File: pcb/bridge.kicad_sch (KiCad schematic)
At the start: 46 parts, among them Q4 IRFR4105, Q5 BC817, Q6 IRFR4105, Q7 BC817, Q8 IRFR4105, Q9 IRFR4105, U1 74HC04, U10 LM75B, U2 74HC04

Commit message: Export root page escription to other pages.
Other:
- company: (none) -> Model Railroader Club Brno I – KMŽ Brno I – https://kmz-brno.cz/
- title: HB22 – bridge -> HB22 – DCC booster
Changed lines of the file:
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@@
 	(paper "A4")
 	(title_block
-		(title "HB22 – bridge")
+		(title "HB22 – DCC booster")
+		(date "2025-02-20")
+		(rev "1.0")
+		(company "Model Railroader Club Brno I – KMŽ Brno I – https://kmz-brno.cz/")
+		(comment 1 "Jan Horáček")
+		(comment 2 "https://github.com/kmzbrnoI/hb22")
+		(comment 3 "https://creativecommons.org/licenses/by-sa/4.0/")
+		(comment 4 "Released under the Creative Commons Attribution-ShareAlike 4.0 License")
 	)
 	(junction

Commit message: Use normal SMD footprints, avoid handsolder.
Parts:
- C10, C11, C12, C13, C15, C8: footprint Capacitor_SMD:C_0805_2012Metric_Pad1.18x1.45mm_HandSolder -> Capacitor_SMD:C_0805_2012Metric
- R17, R18: footprint Resistor_SMD:R_2512_6332Metric_Pad1.40x3.35mm_HandSolder -> Resistor_SMD:R_2512_6332Metric
- R19, R20, R21, R22, R23, R24, R25, R26, R27, R28, R29, R31, R32, R34, R35, R36, R37, R38, R39, R40: footprint Resistor_SMD:R_0805_2012Metric_Pad1.20x1.40mm_HandSolder -> Resistor_SMD:R_0805_2012Metric
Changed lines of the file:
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@@
 			)
 		)
-		(property "Footprint" "Resistor_SMD:R_0805_2012Metric_Pad1.20x1.40mm_HandSolder"
+		(property "Footprint" "Resistor_SMD:R_0805_2012Metric"
 			(at 170.18 129.032 90)
 			(effects
@@
 			)
 		)
-		(property "Footprint" "Resistor_SMD:R_0805_2012Metric_Pad1.20x1.40mm_HandSolder"
+		(property "Footprint" "Resistor_SMD:R_0805_2012Metric"
 			(at 200.66 143.002 90)
 			(effects
@@
 			)
 		)
-		(property "Footprint" "Resistor_SMD:R_0805_2012Metric_Pad1.20x1.40mm_HandSolder"
+		(property "Footprint" "Resistor_SMD:R_0805_2012Metric"
 			(at 200.66 80.518 90)
 			(effects
@@
 			)
 		)
-		(property "Footprint" "Resistor_SMD:R_0805_2012Metric_Pad1.20x1.40mm_HandSolder"
+		(property "Footprint" "Resistor_SMD:R_0805_2012Metric"
 			(at 170.18 62.992 90)
 			(effects
@@
 			)
 		)
-		(property "Footprint" "Resistor_SMD:R_0805_2012Metric_Pad1.20x1.40mm_HandSolder"
+		(property "Footprint" "Resistor_SMD:R_0805_2012Metric"
 			(at 199.39 110.998 90)
 			(effects
@@
 			)
 		)
-		(property "Footprint" "Capacitor_SMD:C_0805_2012Metric_Pad1.18x1.45mm_HandSolder"
+		(property "Footprint" "Capacitor_SMD:C_0805_2012Metric"
 			(at 180.34 110.1852 0)
 			(effects
@@
 			)
 		)
-		(property "Footprint" "Resistor_SMD:R_0805_2012Metric_Pad1.20x1.40mm_HandSolder"
+		(property "Footprint" "Resistor_SMD:R_0805_2012Metric"
 			(at 147.32 79.248 90)
 			(effects
@@
 			)
 		)
-		(property "Footprint" "Resistor_SMD:R_0805_2012Metric_Pad1.20x1.40mm_HandSolder"
+		(property "Footprint" "Resistor_SMD:R_0805_2012Metric"
 			(at 147.32 70.612 90)
 			(effects
@@
 			)
 		)
-		(property "Footprint" "Resistor_SMD:R_0805_2012Metric_Pad1.20x1.40mm_HandSolder"
+		(property "Footprint" "Resistor_SMD:R_0805_2012Metric"
 			(at 147.32 56.642 90)
 			(effects
@@
 			)
 		)
-		(property "Footprint" "Resistor_SMD:R_0805_2012Metric_Pad1.20x1.40mm_HandSolder"
+		(property "Footprint" "Resistor_SMD:R_0805_2012Metric"
 			(at 147.32 51.562 90)
 			(effects
@@
 			)
 		)
-		(property "Footprint" "Capacitor_SMD:C_0805_2012Metric_Pad1.18x1.45mm_HandSolder"
+		(property "Footprint" "Capacitor_SMD:C_0805_2012Metric"
 			(at 228.2952 62.23 0)
 			(effects
@@
 			)
 		)
-		(property "Footprint" "Capacitor_SMD:C_0805_2012Metric_Pad1.18x1.45mm_HandSolder"
+		(property "Footprint" "Capacitor_SMD:C_0805_2012Metric"
 			(at 261.3152 62.23 0)
 			(effects
@@
 			)
 		)
-		(property "Footprint" "Resistor_SMD:R_2512_6332Metric_Pad1.40x3.35mm_HandSolder"
+		(property "Footprint" "Resistor_SMD:R_2512_6332Metric"
 			(at 234.442 44.45 90)
 			(effects
@@
 			)
 		)
-		(property "Footprint" "Resistor_SMD:R_2512_6332Metric_Pad1.40x3.35mm_HandSolder"
+		(property "Footprint" "Resistor_SMD:R_2512_6332Metric"
 			(at 267.462 44.45 90)
 			(effects
@@
 			)
 		)
-		(property "Footprint" "Resistor_SMD:R_0805_2012Metric_Pad1.20x1.40mm_HandSolder"
+		(property "Footprint" "Resistor_SMD:R_0805_2012Metric"
 			(at 147.32 145.288 90)
 			(effects
@@
 			)
 		)
-		(property "Footprint" "Resistor_SMD:R_0805_2012Metric_Pad1.20x1.40mm_HandSolder"
+		(property "Footprint" "Resistor_SMD:R_0805_2012Metric"
 			(at 147.32 136.652 90)
 			(effects
@@
 			)
 		)
-		(property "Footprint" "Resistor_SMD:R_0805_2012Metric_Pad1.20x1.40mm_HandSolder"
+		(property "Footprint" "Resistor_SMD:R_0805_2012Metric"
 			(at 147.32 122.682 90)
 			(effects
@@
 			)
 		)
-		(property "Footprint" "Resistor_SMD:R_0805_2012Metric_Pad1.20x1.40mm_HandSolder"
+		(property "Footprint" "Resistor_SMD:R_0805_2012Metric"
 			(at 147.32 117.602 90)
 			(effects
@@
 			)
 		)
-		(property "Footprint" "Resistor_SMD:R_0805_2012Metric_Pad1.20x1.40mm_HandSolder"
+		(property "Footprint" "Resistor_SMD:R_0805_2012Metric"
 			(at 74.422 48.26 90)
 			(effects
@@
 			)
 		)
-		(property "Footprint" "Resistor_SMD:R_0805_2012Metric_Pad1.20x1.40mm_HandSolder"
+		(property "Footprint" "Resistor_SMD:R_0805_2012Metric"
 			(at 69.342 48.26 90)
 			(effects
@@
 			)
 		)
-		(property "Footprint" "Resistor_SMD:R_0805_2012Metric_Pad1.20x1.40mm_HandSolder"
+		(property "Footprint" "Resistor_SMD:R_0805_2012Metric"
 			(at 35.56 69.342 90)
 			(effects
@@
 			)
 		)
-		(property "Footprint" "Resistor_SMD:R_0805_2012Metric_Pad1.20x1.40mm_HandSolder"
+		(property "Footprint" "Resistor_SMD:R_0805_2012Metric"
 			(at 35.56 85.852 90)
 			(effects
@@
 			)
 		)
-		(property "Footprint" "Resistor_SMD:R_0805_2012Metric_Pad1.20x1.40mm_HandSolder"
+		(property "Footprint" "Resistor_SMD:R_0805_2012Metric"
 			(at 65.532 99.06 90)
 			(effects
@@
 			)
 		)
-		(property "Footprint" "Resistor_SMD:R_0805_2012Metric_Pad1.20x1.40mm_HandSolder"
+		(property "Footprint" "Resistor_SMD:R_0805_2012Metric"
 			(at 65.532 111.76 90)
 			(effects
@@
 			)
 		)
-		(property "Footprint" "Capacitor_SMD:C_0805_2012Metric_Pad1.18x1.45mm_HandSolder"
+		(property "Footprint" "Capacitor_SMD:C_0805_2012Metric"
 			(at 61.9252 107.95 0)
 			(effects
@@
 			)
 		)
-		(property "Footprint" "Capacitor_SMD:C_0805_2012Metric_Pad1.18x1.45mm_HandSolder"
+		(property "Footprint" "Capacitor_SMD:C_0805_2012Metric"
 			(at 163.5252 30.48 0)
 			(effects
@@
 			)
 		)
-		(property "Footprint" "Capacitor_SMD:C_0805_2012Metric_Pad1.18x1.45mm_HandSolder"
+		(property "Footprint" "Capacitor_SMD:C_0805_2012Metric"
 			(at 84.7852 163.83 0)
 			(effects
@@
 			)
 		)
-		(property "Footprint" "Resistor_SMD:R_0805_2012Metric_Pad1.20x1.40mm_HandSolder"
+		(property "Footprint" "Resistor_SMD:R_0805_2012Metric"
 			(at 66.802 170.18 90)
 			(effects

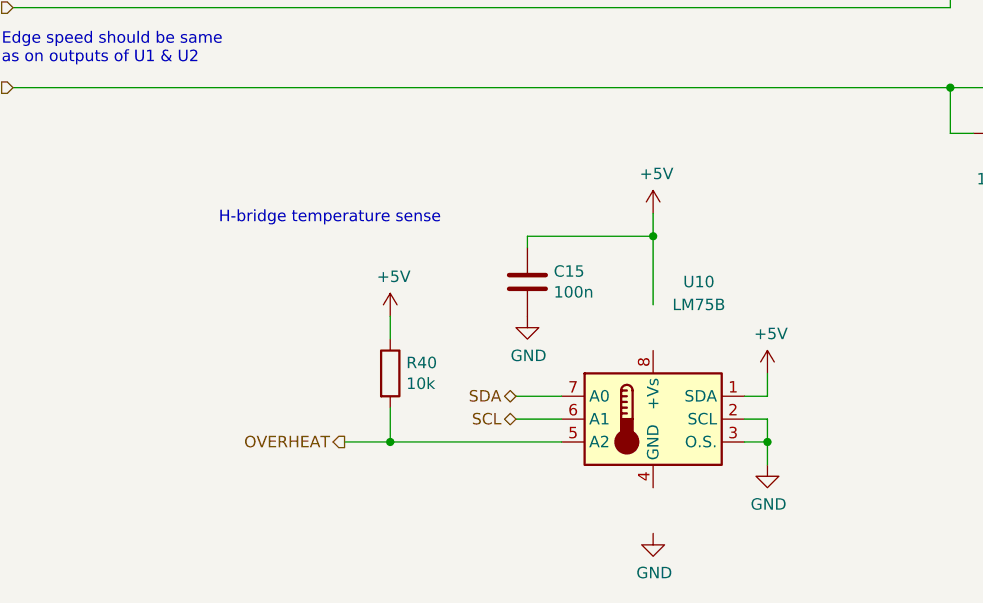
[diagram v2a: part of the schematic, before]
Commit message: Add stabil heatsinks, minor improvements.
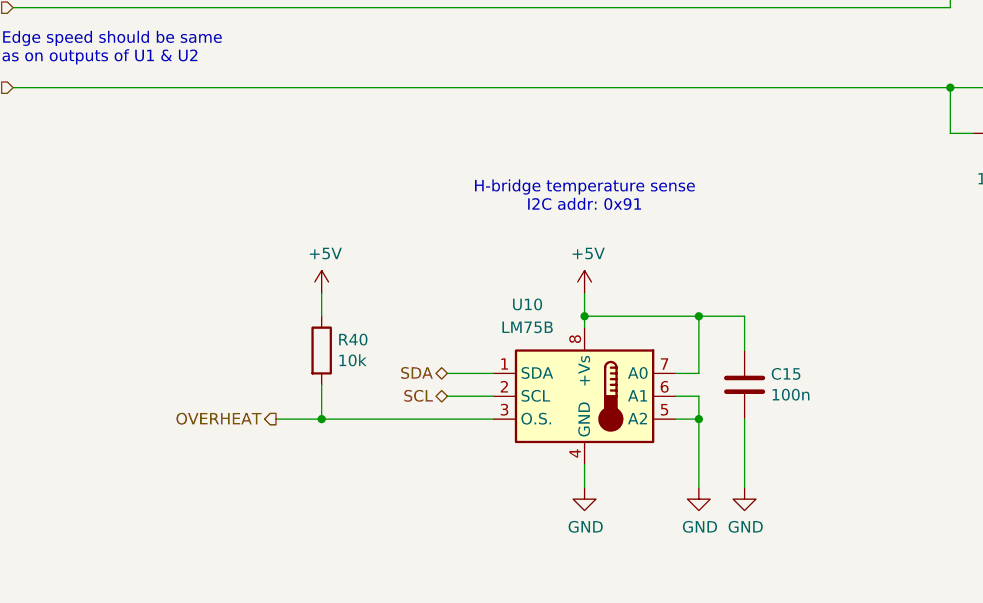
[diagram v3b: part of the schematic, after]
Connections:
- net +5V: now also U10.7 (A0), U10.8 (+Vs); no longer U10.1 (SDA)
- net GND: now also U10.4 (GND), U10.5 (A2), U10.6 (A1); no longer U10.2 (SCL), U10.3 (O.S.)
- net OVERHEAT: now also U10.3 (O.S.); no longer U10.5 (A2)
- net SCL: now also U10.2 (SCL); no longer U10.6 (A1)
- net SDA: now also U10.1 (SDA); no longer U10.7 (A0)
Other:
- note added: "H-bridge temperature sense I2C addr: 0x91"
- note removed: "H-bridge temperature sense"
- moved on the sheet: C15, R40, U10

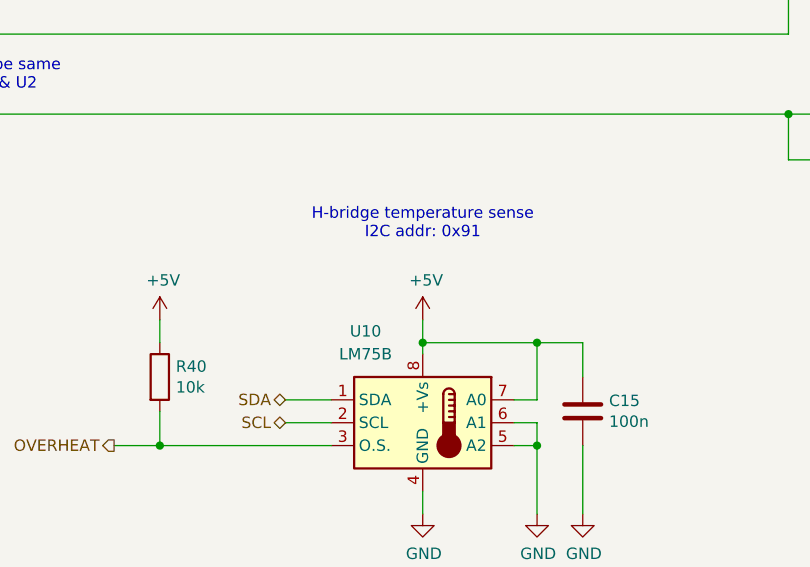
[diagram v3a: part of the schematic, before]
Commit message: Add temp. sensor for current limiter.
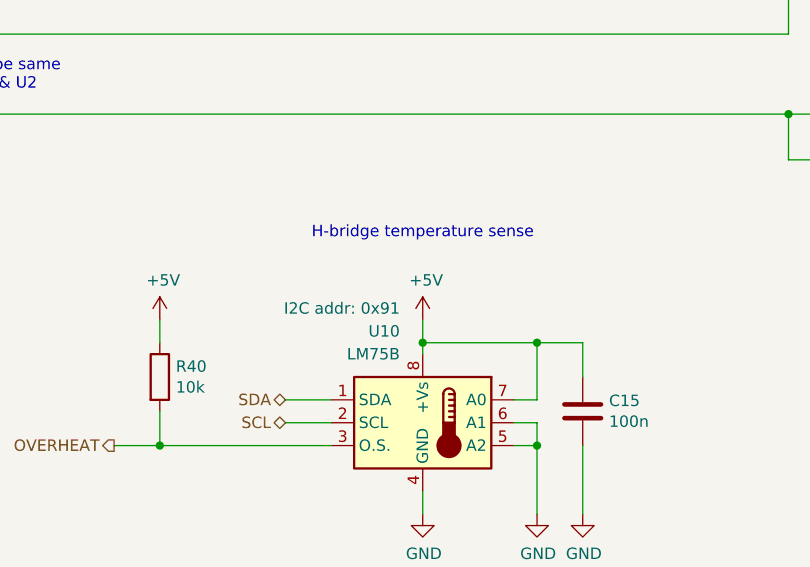
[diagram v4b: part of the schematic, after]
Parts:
- U10: I2C addr (none) -> 0x91
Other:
- note added: "H-bridge temperature sense"
- note removed: "H-bridge temperature sense I2C addr: 0x91"
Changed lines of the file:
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@@
 		)
 	)
-	(text "H-bridge temperature sense\nI2C addr: 0x91"
+	(text "H-bridge temperature sense"
 		(exclude_from_sim no)
 		(at 90.17 152.4 0)
@@
 		(dnp no)
 		(property "Reference" "U10"
-			(at 83.82 162.56 0)
+			(at 87.63 162.56 0)
 			(effects
 				(font
 					(size 1.27 1.27)
 				)
+				(justify left)
 			)
 		)
 		(property "Value" "LM75B"
-			(at 83.82 165.1 0)
+			(at 87.63 165.1 0)
 			(effects
 				(font
 					(size 1.27 1.27)
 				)
+				(justify left)
 			)
 		)
@@
 			)
 		)
+		(property "I2C addr" "0x91"
+			(at 87.63 160.02 0)
+			(show_name yes)
+			(effects
+				(font
+					(size 1.27 1.27)
+				)
+				(justify left)
+			)
+		)

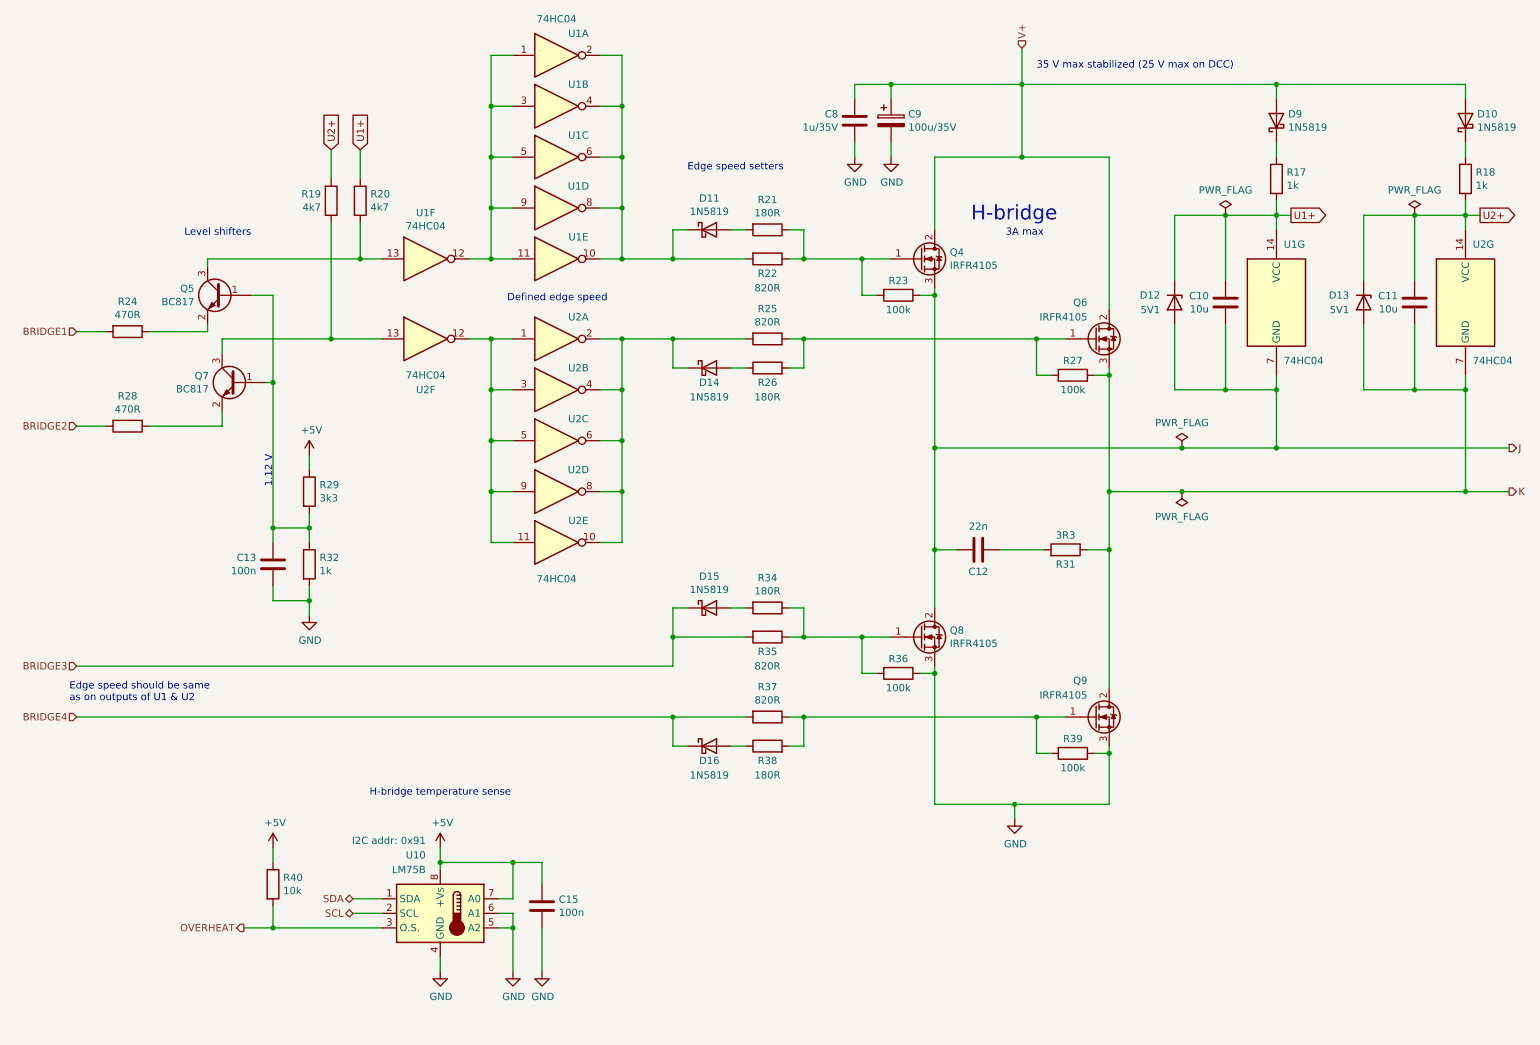
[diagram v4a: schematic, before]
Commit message: Add heasinks to output bridge.
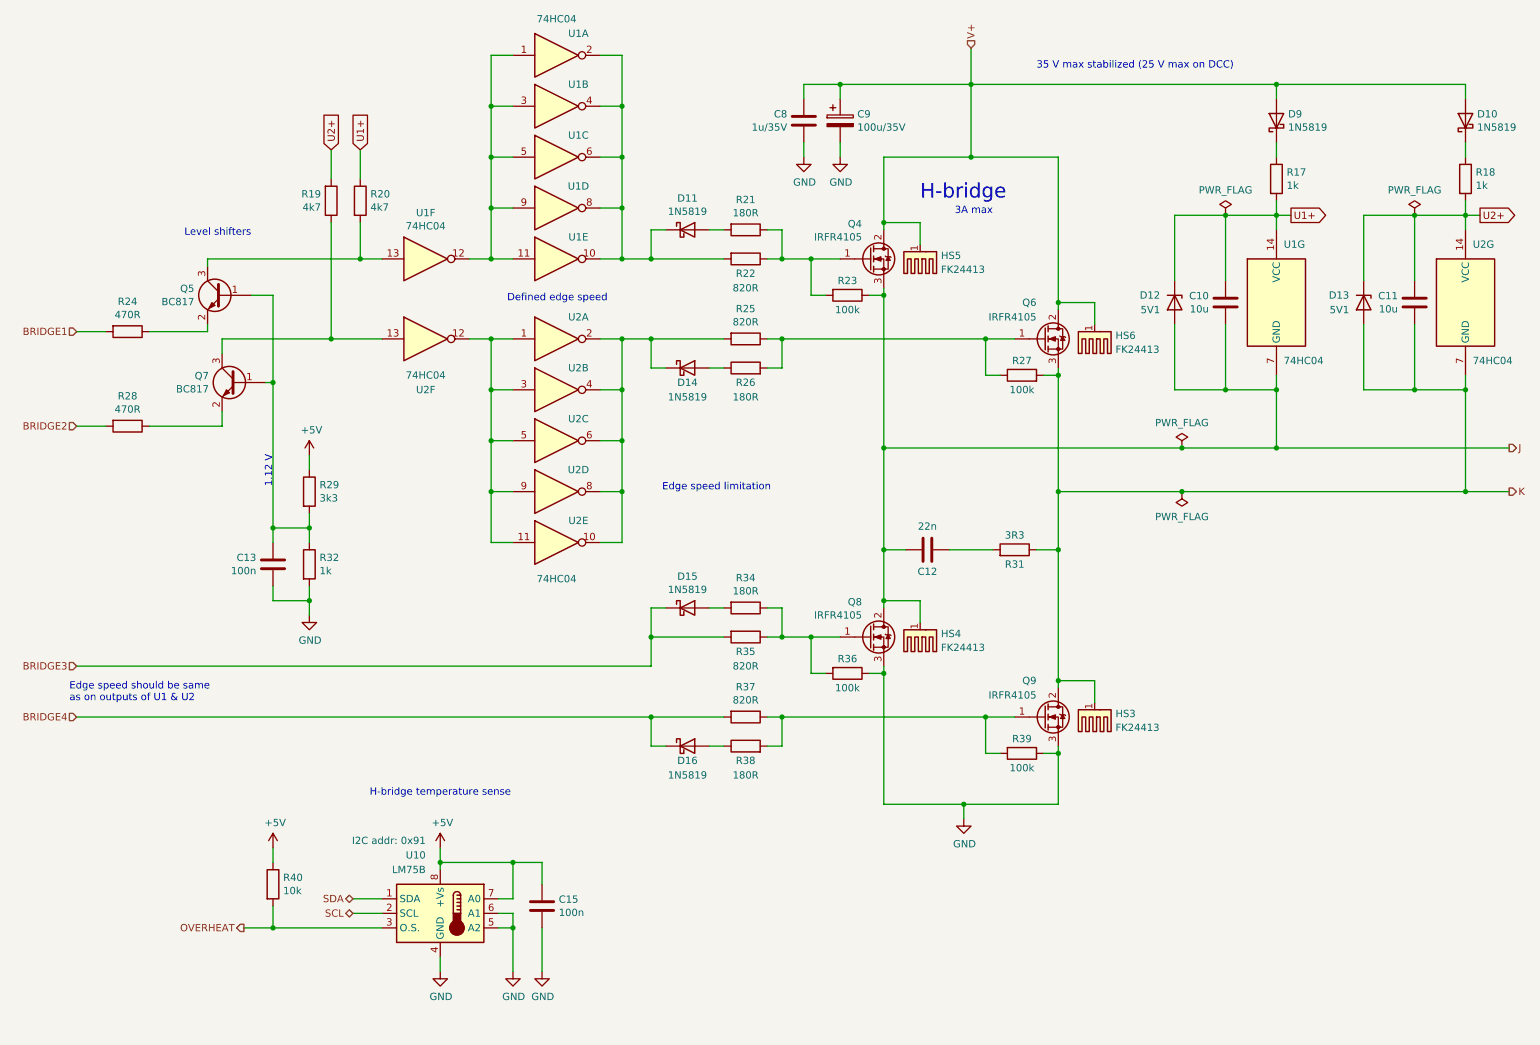
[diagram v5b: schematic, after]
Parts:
- added HS3, HS4, HS5, HS6: FK24413, symbol Mechanical:Heatsink_Pad
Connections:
- net J: now also HS4.1
- net K: now also HS3.1
- net V+: now also HS5.1, HS6.1
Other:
- note added: "Edge speed limitation"
- note removed: "Edge speed setters"
- moved on the sheet: C12, C8, C9, D11, D14, D15, D16, Q4, Q6, Q8, Q9, R21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
